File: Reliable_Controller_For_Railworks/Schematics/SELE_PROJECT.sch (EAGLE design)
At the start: 21 parts, among them IC1 24LC1025, IC2 MAX232, U1 328P, U2 LTC485N, U3 LTC485N, X1 16MHz

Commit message: updated electrical schematic
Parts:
- removed C8: 1u, rcl:EL-BI25-10AXIAL
- removed PC: DB9 CONNECTOR, pinhead:PINHD-1X9
- removed R5: 120, eagle-ltspice:R
- removed U3: LTC485N, linear-technology:LTC485N
- added D1, D2, D3, D4: 1N4148DO35-7, diode:1N4148DO35-7
- added IC3: 7805L, linear:7805L
- added TR1: SM-EP7, inductor-neosid:SM-EP7
- added X2: (no value), con-phoenix-254:MPT2
- added X4: 6ESRM-P, con-tycoelectronics:6ESRM-P
- C5: value 1u -> 1500u/35V; device rcl:EL-BI25-10AXIAL -> rcl:CPOL-EU150CLZ-1010
- C6, C7: value 1u -> 0.1u; device rcl:EL-BI25-10AXIAL -> eagle-ltspice:CC1210
- IC2: value MAX232 -> 7812L; device maxim:MAX232 -> linear:7812L
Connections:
- removed net N$15: C6.2, IC2G$1.C2-
- removed net N$19: C8.2, IC2G$1.V-
- removed net RTS: IC2G$1.R2IN, PC.7
- removed net RXD: IC2G$1.T1OUT, PC.2
- removed net TXD: IC2G$1.R1IN, PC.3
- net GND: now also C5.-, C6.2, C7.2, D1.A, D2.A, IC2.GND, IC3.GND; no longer C8.1, U3.GND
- net N$11: now also D1.C, D4.A, TR1.6; no longer IC2G$1.T1IN, U3.RO
- net N$12: now also D2.C, D3.A, TR1.4; no longer IC2G$1.R1OUT, U3.DI
- net N$13: now also TR1.1, X4.AC1; no longer IC2G$1.R2OUT, U3.!RE, U3.DE
- net N$14: now also TR1.3, X4.AC2; no longer C5.1, IC2G$1.C1+
- net N$16: now also C5.+, C7.1, D3.C, D4.C, IC2.VI; no longer C6.1, IC2G$1.C2+
- net N$17: now also TR1.2, X4.SH; no longer C5.2, IC2G$1.C1-
- net N$18: now also C6.1, IC2.VO, IC3.VI; no longer C7.2, IC2G$1.V+
- net N$6: now also X2-1.1; no longer R5.1, U3.A
- net N$9: now also X2-2.1; no longer R5.2, U3.B
- net VCC: now also IC3.VO; no longer C7.1, U3.VCC
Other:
- moved on the sheet: R4

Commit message: schematic update
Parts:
- T1: value SM-EP7 -> 230V to 12V AC
- renumbered TR1 to T1
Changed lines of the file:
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@@
 <part name="D4" library="diode" library_urn="urn:adsk.eagle:library:210" deviceset="1N4148" device="DO35-7" package3d_urn="urn:adsk.eagle:package:43339/1"/>
 <part name="D1" library="diode" library_urn="urn:adsk.eagle:library:210" deviceset="1N4148" device="DO35-7" package3d_urn="urn:adsk.eagle:package:43339/1"/>
-<part name="TR1" library="inductor-neosid" library_urn="urn:adsk.eagle:library:241" deviceset="SM-EP" device="7" package3d_urn="urn:adsk.eagle:package:14729/1"/>
+<part name="T1" library="inductor-neosid" library_urn="urn:adsk.eagle:library:241" deviceset="SM-EP" device="7" package3d_urn="urn:adsk.eagle:package:14729/1" value="230V to 12V AC"/>
 <part name="IC2" library="linear" library_urn="urn:adsk.eagle:library:262" deviceset="78*" device="L" package3d_urn="urn:adsk.eagle:package:16416/2" technology="12"/>
 <part name="IC3" library="linear" library_urn="urn:adsk.eagle:library:262" deviceset="78*" device="L" package3d_urn="urn:adsk.eagle:package:16416/2" technology="05"/>
@@
 <attribute name="VALUE" x="71.12" y="144.5514" size="1.778" layer="96" rot="R180"/>
 </instance>
-<instance part="TR1" gate="G$1" x="45.72" y="137.16">
+<instance part="T1" gate="G$1" x="45.72" y="137.16">
 <attribute name="NAME" x="43.18" y="146.558" size="1.778" layer="95"/>
-<attribute name="VALUE" x="43.18" y="126.492" size="1.778" layer="96"/>
+<attribute name="VALUE" x="33.02" y="126.492" size="1.778" layer="96"/>
 </instance>
 <instance part="IC2" gate="A1" x="134.62" y="137.16">
@@
 <attribute name="VALUE" x="100.203" y="119.8626" size="1.778" layer="96"/>
 </instance>
-<instance part="GND9" gate="1" x="173.99" y="104.14">
-<attribute name="VALUE" x="171.45" y="101.6" size="1.778" layer="96"/>
+<instance part="GND9" gate="1" x="201.93" y="104.14">
+<attribute name="VALUE" x="199.39" y="101.6" size="1.778" layer="96"/>
 </instance>
 <instance part="P+7" gate="VCC" x="199.39" y="153.67">
@@
 <pinref part="IC3" gate="A1" pin="GND"/>
 <wire x1="134.62" y1="106.68" x2="147.32" y2="106.68" width="0.1524" layer="91"/>
-<wire x1="147.32" y1="106.68" x2="173.99" y2="106.68" width="0.1524" layer="91"/>
-<wire x1="173.99" y1="106.68" x2="175.26" y2="106.68" width="0.1524" layer="91"/>
+<wire x1="147.32" y1="106.68" x2="201.93" y2="106.68" width="0.1524" layer="91"/>
+<wire x1="201.93" y1="106.68" x2="175.26" y2="106.68" width="0.1524" layer="91"/>
 <wire x1="175.26" y1="106.68" x2="175.26" y2="129.54" width="0.1524" layer="91"/>
 <junction x="134.62" y="106.68"/>
 <pinref part="GND9" gate="1" pin="GND"/>
-<junction x="173.99" y="106.68"/>
+<junction x="201.93" y="106.68"/>
 <pinref part="C7" gate="G$1" pin="2"/>
 <wire x1="121.92" y1="119.38" x2="121.92" y2="106.68" width="0.1524" layer="91"/>
@@
 <net name="N$11" class="0">
 <segment>
-<pinref part="TR1" gate="G$1" pin="6"/>
+<pinref part="T1" gate="G$1" pin="6"/>
 <wire x1="50.8" y1="144.78" x2="50.8" y2="149.86" width="0.1524" layer="91"/>
 <pinref part="D4" gate="G$1" pin="A"/>
@@
 <net name="N$12" class="0">
 <segment>
-<pinref part="TR1" gate="G$1" pin="4"/>
+<pinref part="T1" gate="G$1" pin="4"/>
 <wire x1="50.8" y1="129.54" x2="50.8" y2="124.46" width="0.1524" layer="91"/>
 <wire x1="50.8" y1="124.46" x2="60.96" y2="124.46" width="0.1524" layer="91"/>
@@
 <net name="N$13" class="0">
 <segment>
-<pinref part="TR1" gate="G$1" pin="1"/>
+<pinref part="T1" gate="G$1" pin="1"/>
 <wire x1="40.64" y1="144.78" x2="20.32" y2="144.78" width="0.1524" layer="91"/>
 <pinref part="X4" gate="G$1" pin="AC1"/>
@@
 <net name="N$14" class="0">
 <segment>
-<pinref part="TR1" gate="G$1" pin="3"/>
+<pinref part="T1" gate="G$1" pin="3"/>
 <wire x1="40.64" y1="129.54" x2="20.32" y2="129.54" width="0.1524" layer="91"/>
 <pinref part="X4" gate="G$1" pin="AC2"/>
@@
 <segment>
 <pinref part="X4" gate="G$1" pin="SH"/>
-<pinref part="TR1" gate="G$1" pin="2"/>
+<pinref part="T1" gate="G$1" pin="2"/>
 <wire x1="20.32" y1="137.16" x2="40.64" y2="137.16" width="0.1524" layer="91"/>
 </segment>

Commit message: updated schematic
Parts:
- IC1: value 24LC1025 -> D1 (24LC1025)
- IC2: value 7812L -> D2 (7812L)
- IC3: value 7805L -> D3 (7805L)
- renumbered D1 to V1, D2 to V2, D3 to V3, D4 to V4
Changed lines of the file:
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@@
 <part name="GND6" library="SBMI" deviceset="GND" device=""/>
 <part name="X1" library="special" library_urn="urn:adsk.eagle:library:367" deviceset="XTAL" device="" package3d_urn="urn:adsk.eagle:package:26649/1" value="16MHz"/>
-<part name="IC1" library="atmel" library_urn="urn:adsk.eagle:library:105" deviceset="AT24C*" device="P" package3d_urn="urn:adsk.eagle:package:4324/1" value="24LC1025"/>
+<part name="IC1" library="atmel" library_urn="urn:adsk.eagle:library:105" deviceset="AT24C*" device="P" package3d_urn="urn:adsk.eagle:package:4324/1" value="D1 (24LC1025)"/>
 <part name="GND5" library="SBMI" deviceset="GND" device=""/>
 <part name="GND7" library="SBMI" deviceset="GND" device=""/>
@@
 <part name="P+6" library="SBMI" deviceset="VCC" device=""/>
 <part name="X2" library="con-phoenix-254" deviceset="MPT2" device=""/>
-<part name="D2" library="diode" library_urn="urn:adsk.eagle:library:210" deviceset="1N4148" device="DO35-7" package3d_urn="urn:adsk.eagle:package:43339/1"/>
-<part name="D3" library="diode" library_urn="urn:adsk.eagle:library:210" deviceset="1N4148" device="DO35-7" package3d_urn="urn:adsk.eagle:package:43339/1"/>
-<part name="D4" library="diode" library_urn="urn:adsk.eagle:library:210" deviceset="1N4148" device="DO35-7" package3d_urn="urn:adsk.eagle:package:43339/1"/>
-<part name="D1" library="diode" library_urn="urn:adsk.eagle:library:210" deviceset="1N4148" device="DO35-7" package3d_urn="urn:adsk.eagle:package:43339/1"/>
+<part name="V2" library="diode" library_urn="urn:adsk.eagle:library:210" deviceset="1N4148" device="DO35-7" package3d_urn="urn:adsk.eagle:package:43339/1"/>
+<part name="V3" library="diode" library_urn="urn:adsk.eagle:library:210" deviceset="1N4148" device="DO35-7" package3d_urn="urn:adsk.eagle:package:43339/1"/>
+<part name="V4" library="diode" library_urn="urn:adsk.eagle:library:210" deviceset="1N4148" device="DO35-7" package3d_urn="urn:adsk.eagle:package:43339/1"/>
+<part name="V1" library="diode" library_urn="urn:adsk.eagle:library:210" deviceset="1N4148" device="DO35-7" package3d_urn="urn:adsk.eagle:package:43339/1"/>
 <part name="T1" library="inductor-neosid" library_urn="urn:adsk.eagle:library:241" deviceset="SM-EP" device="7" package3d_urn="urn:adsk.eagle:package:14729/1" value="230V to 12V AC"/>
-<part name="IC2" library="linear" library_urn="urn:adsk.eagle:library:262" deviceset="78*" device="L" package3d_urn="urn:adsk.eagle:package:16416/2" technology="12"/>
-<part name="IC3" library="linear" library_urn="urn:adsk.eagle:library:262" deviceset="78*" device="L" package3d_urn="urn:adsk.eagle:package:16416/2" technology="05"/>
+<part name="IC2" library="linear" library_urn="urn:adsk.eagle:library:262" deviceset="78*" device="L" package3d_urn="urn:adsk.eagle:package:16416/2" technology="12" value="D2 (7812L)"/>
+<part name="IC3" library="linear" library_urn="urn:adsk.eagle:library:262" deviceset="78*" device="L" package3d_urn="urn:adsk.eagle:package:16416/2" technology="05" value="D3 (7805L)"/>
 <part name="C5" library="rcl" library_urn="urn:adsk.eagle:library:334" deviceset="CPOL-EU" device="150CLZ-1010" package3d_urn="urn:adsk.eagle:package:23403/1" value="1500u/35V"/>
 <part name="GND9" library="SBMI" deviceset="GND" device=""/>
@@
 <attribute name="VALUE" x="197.104" y="197.358" size="1.778" layer="96"/>
 </instance>
-<instance part="D2" gate="G$1" x="73.66" y="132.08" rot="R180">
+<instance part="V2" gate="G$1" x="73.66" y="132.08" rot="R180">
 <attribute name="NAME" x="71.12" y="131.5974" size="1.778" layer="95" rot="R180"/>
 <attribute name="VALUE" x="71.12" y="134.3914" size="1.778" layer="96" rot="R180"/>
 </instance>
-<instance part="D3" gate="G$1" x="73.66" y="124.46">
+<instance part="V3" gate="G$1" x="73.66" y="124.46">
 <attribute name="NAME" x="76.2" y="124.9426" size="1.778" layer="95"/>
 <attribute name="VALUE" x="76.2" y="122.1486" size="1.778" layer="96"/>
 </instance>
-<instance part="D4" gate="G$1" x="73.66" y="149.86">
+<instance part="V4" gate="G$1" x="73.66" y="149.86">
 <attribute name="NAME" x="76.2" y="150.3426" size="1.778" layer="95"/>
 <attribute name="VALUE" x="76.2" y="147.5486" size="1.778" layer="96"/>
 </instance>
-<instance part="D1" gate="G$1" x="73.66" y="142.24" rot="R180">
+<instance part="V1" gate="G$1" x="73.66" y="142.24" rot="R180">
 <attribute name="NAME" x="71.12" y="141.7574" size="1.778" layer="95" rot="R180"/>
 <attribute name="VALUE" x="71.12" y="144.5514" size="1.778" layer="96" rot="R180"/>
@@
 </segment>
 <segment>
-<pinref part="D1" gate="G$1" pin="A"/>
+<pinref part="V1" gate="G$1" pin="A"/>
 <wire x1="76.2" y1="142.24" x2="81.28" y2="142.24" width="0.1524" layer="91"/>
 <wire x1="81.28" y1="142.24" x2="81.28" y2="137.16" width="0.1524" layer="91"/>
-<pinref part="D2" gate="G$1" pin="A"/>
+<pinref part="V2" gate="G$1" pin="A"/>
 <wire x1="81.28" y1="137.16" x2="81.28" y2="132.08" width="0.1524" layer="91"/>
 <wire x1="81.28" y1="132.08" x2="76.2" y2="132.08" width="0.1524" layer="91"/>
@@
 <pinref part="T1" gate="G$1" pin="6"/>
 <wire x1="50.8" y1="144.78" x2="50.8" y2="149.86" width="0.1524" layer="91"/>
-<pinref part="D4" gate="G$1" pin="A"/>
+<pinref part="V4" gate="G$1" pin="A"/>
 <wire x1="50.8" y1="149.86" x2="60.96" y2="149.86" width="0.1524" layer="91"/>
-<pinref part="D1" gate="G$1" pin="C"/>
+<pinref part="V1" gate="G$1" pin="C"/>
 <wire x1="60.96" y1="149.86" x2="71.12" y2="149.86" width="0.1524" layer="91"/>
 <wire x1="71.12" y1="142.24" x2="60.96" y2="142.24" width="0.1524" layer="91"/>
@@
 <wire x1="50.8" y1="129.54" x2="50.8" y2="124.46" width="0.1524" layer="91"/>
 <wire x1="50.8" y1="124.46" x2="60.96" y2="124.46" width="0.1524" layer="91"/>
-<pinref part="D3" gate="G$1" pin="A"/>
-<pinref part="D2" gate="G$1" pin="C"/>
+<pinref part="V3" gate="G$1" pin="A"/>
+<pinref part="V2" gate="G$1" pin="C"/>
 <wire x1="60.96" y1="124.46" x2="71.12" y2="124.46" width="0.1524" layer="91"/>
 <wire x1="71.12" y1="132.08" x2="60.96" y2="132.08" width="0.1524" layer="91"/>
@@
 <net name="N$16" class="0">
 <segment>
-<pinref part="D3" gate="G$1" pin="C"/>
+<pinref part="V3" gate="G$1" pin="C"/>
 <wire x1="76.2" y1="124.46" x2="104.14" y2="124.46" width="0.1524" layer="91"/>
 <wire x1="104.14" y1="124.46" x2="104.14" y2="137.16" width="0.1524" layer="91"/>
-<pinref part="D4" gate="G$1" pin="C"/>
+<pinref part="V4" gate="G$1" pin="C"/>
 <wire x1="104.14" y1="137.16" x2="104.14" y2="149.86" width="0.1524" layer="91"/>
 <wire x1="104.14" y1="149.86" x2="76.2" y2="149.86" width="0.1524" layer="91"/>

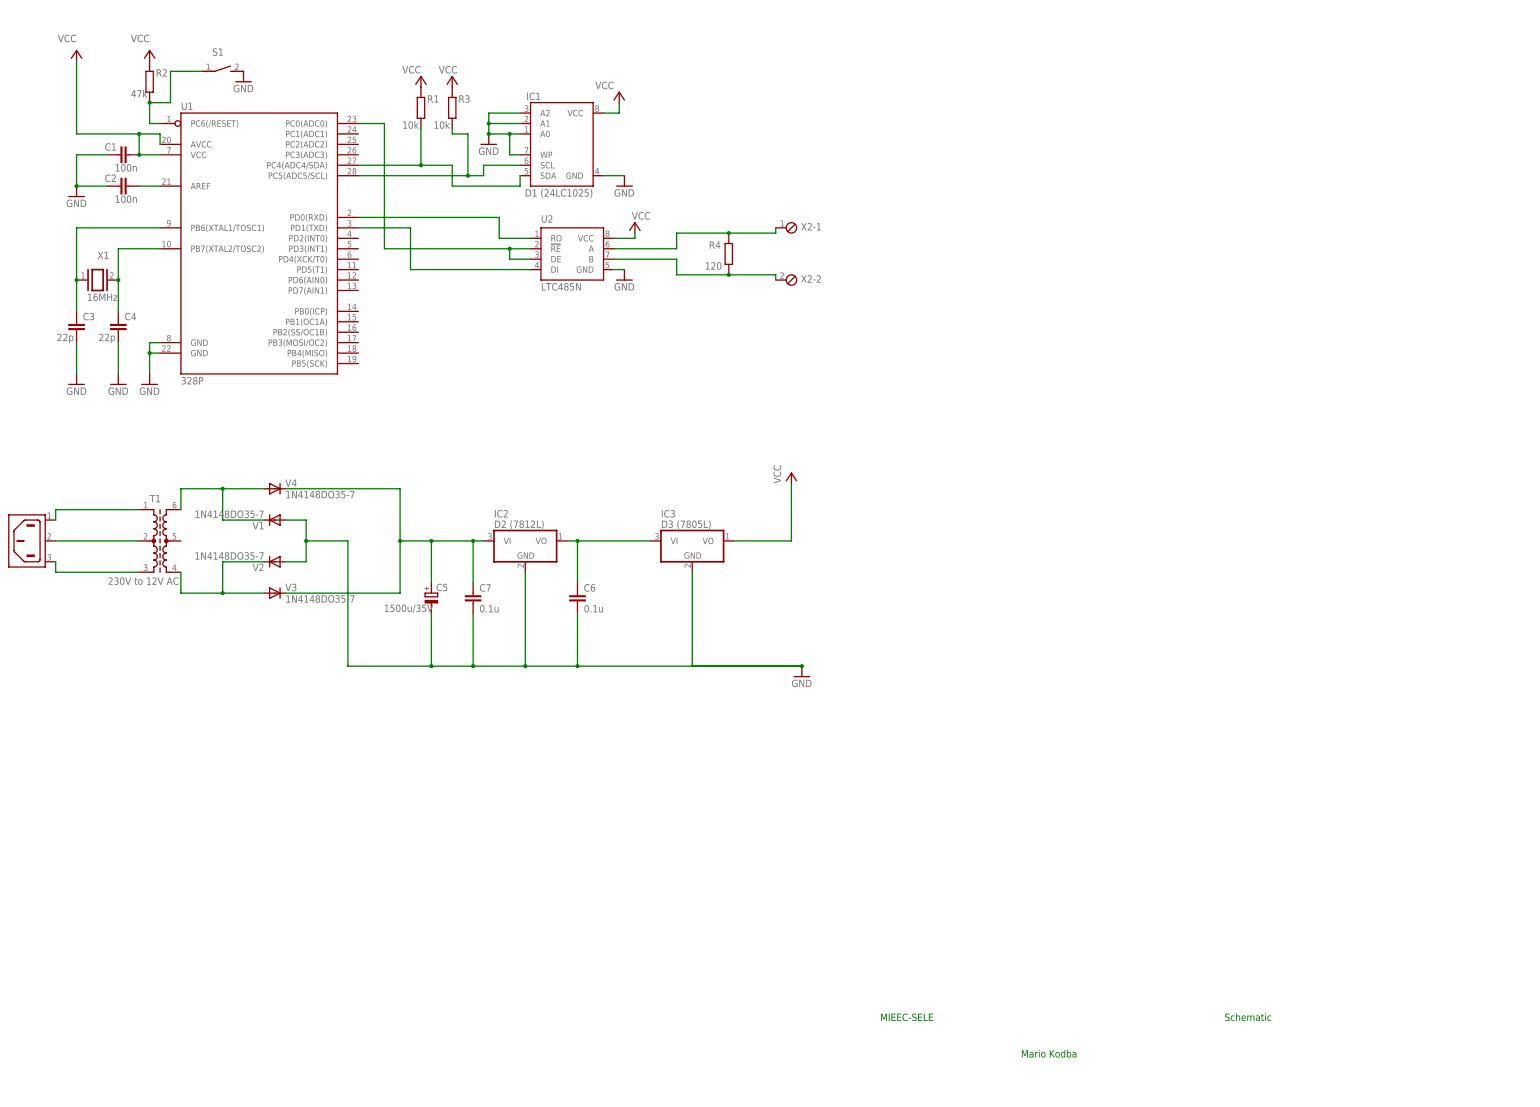
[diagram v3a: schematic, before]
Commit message: Minor bug fix and implementation of log printing in a server command
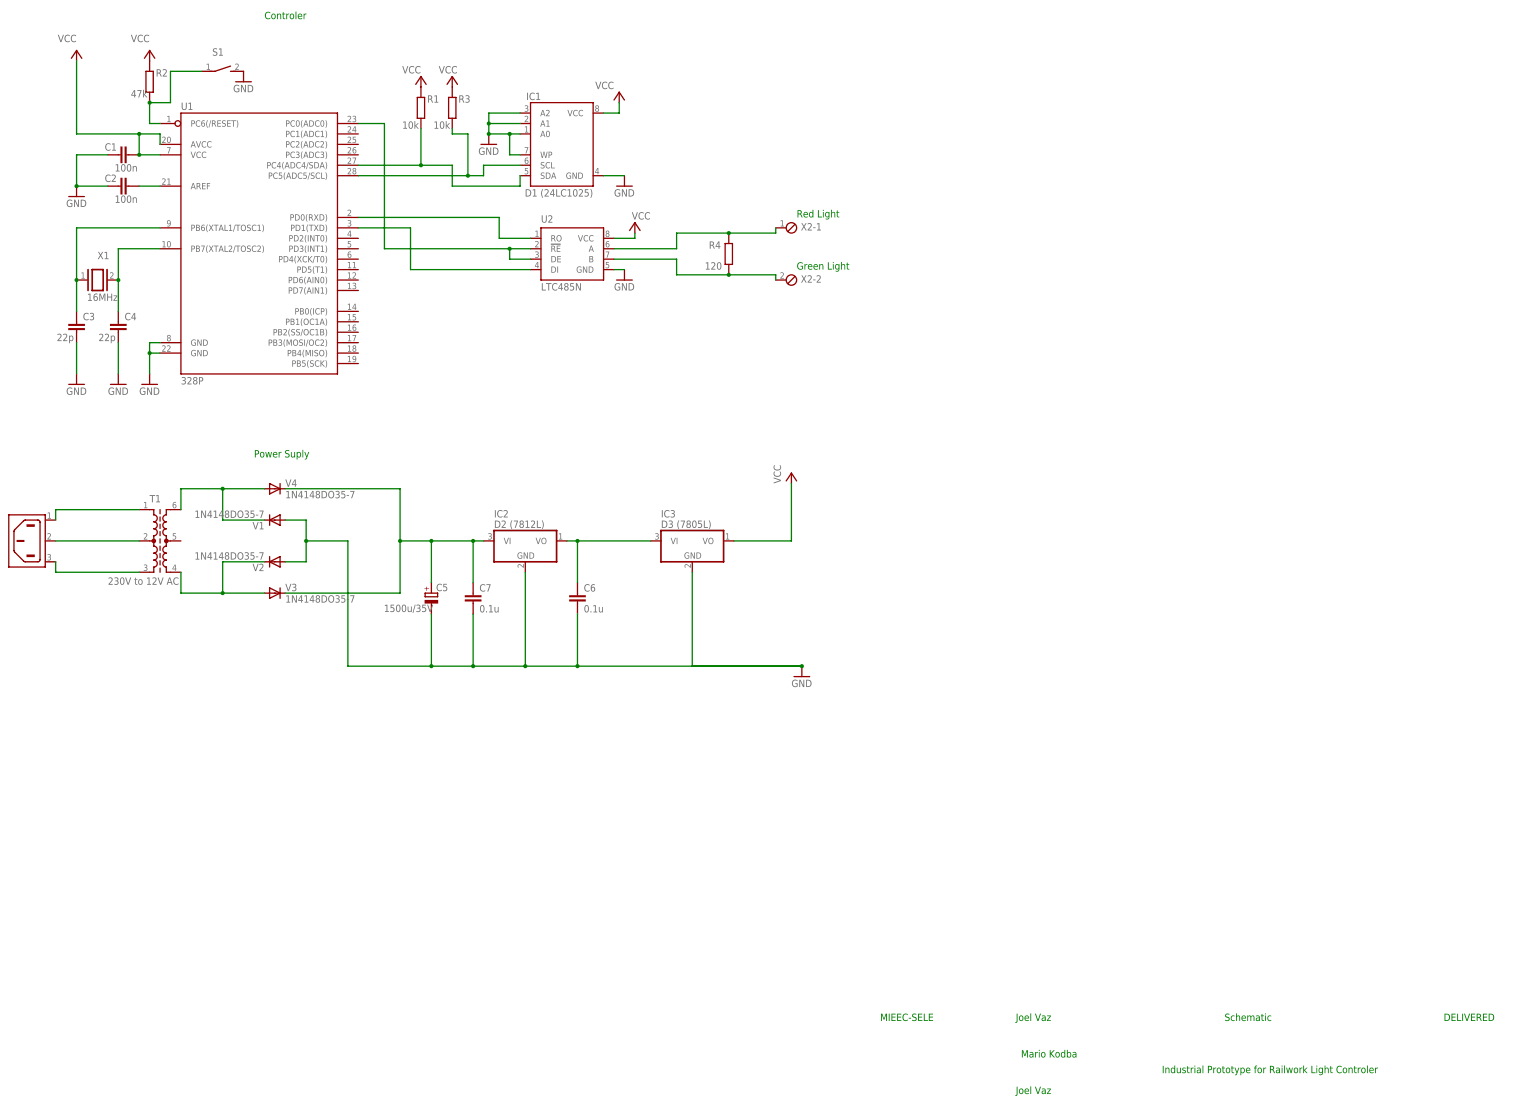
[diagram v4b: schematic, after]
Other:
- note added: "Controler"
- note added: "DELIVERED"
- note added: "Green Light"
- note added: "Industrial Prototype for Railwork Light Controler"
- note added: "Joel Vaz"
- note added: "Power Suply"
- note added: "Red Light"
